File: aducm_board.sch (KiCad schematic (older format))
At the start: 49 parts, among them U1 aducm_355

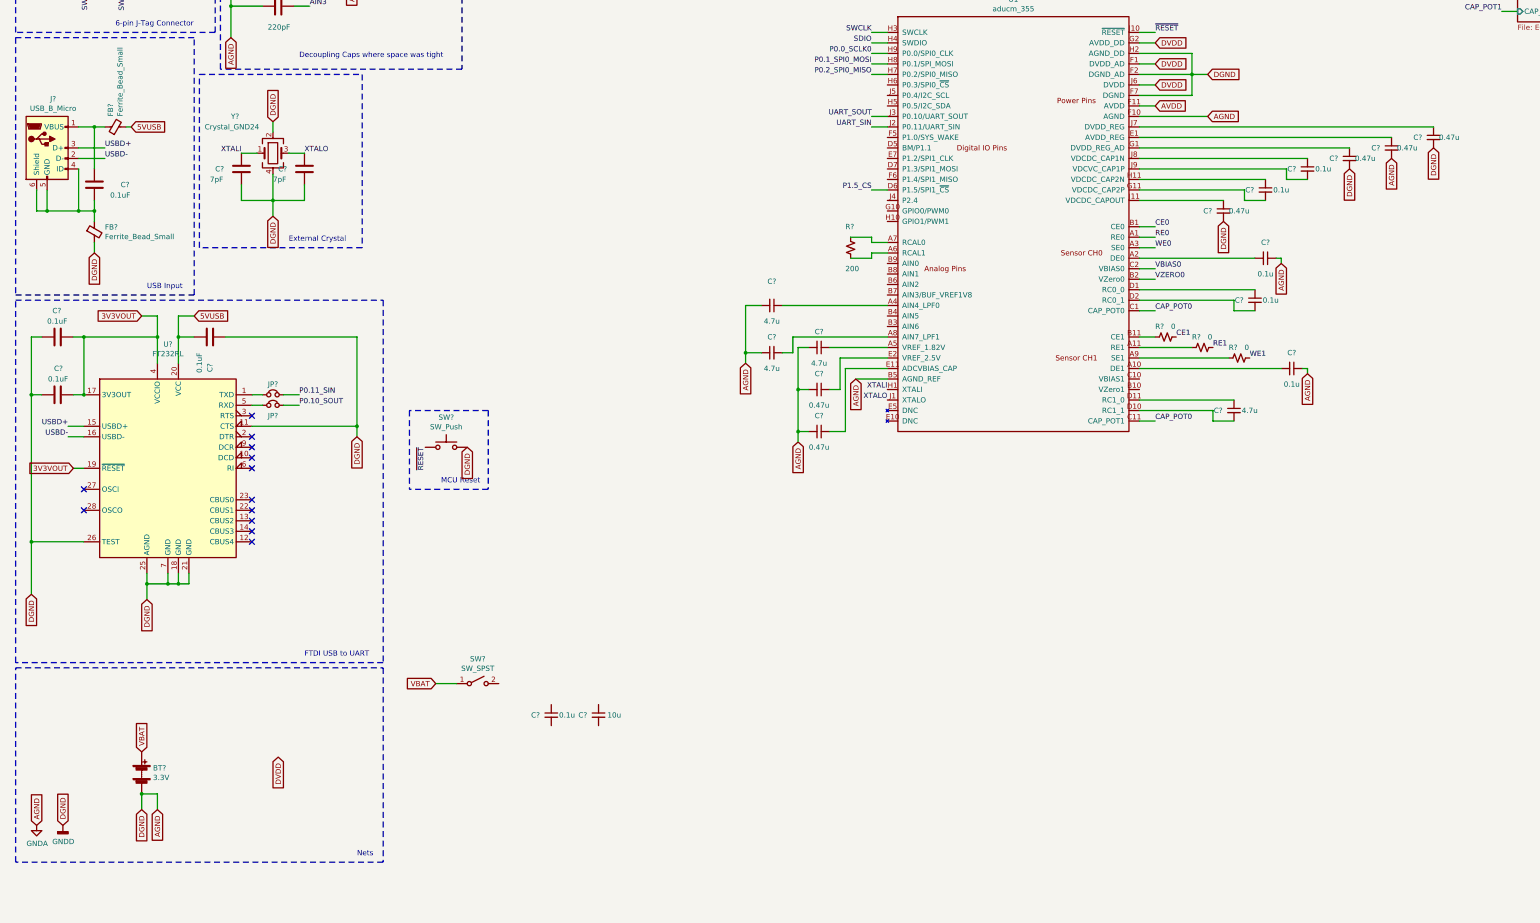
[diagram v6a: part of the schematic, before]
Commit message: Completed Power Supply Filtering
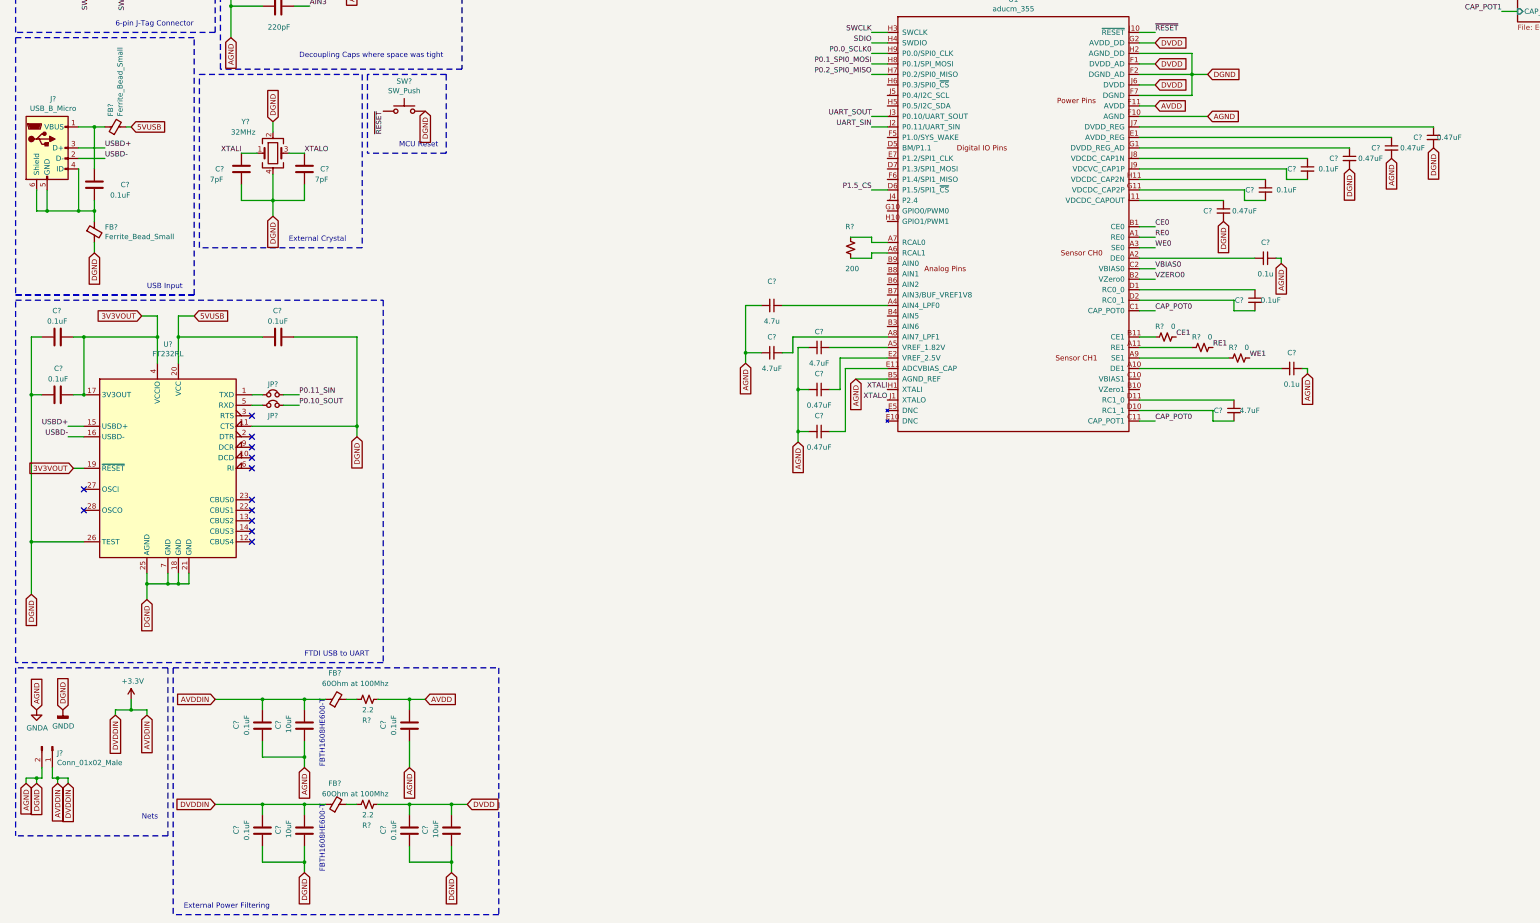
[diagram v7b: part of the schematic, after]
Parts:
- removed BT?: 3.3V, symbol Device:Battery
- removed C?: 0.1u, symbol Device:C_Small
- removed C?: 10u, symbol Device:C_Small
- removed SW?: SW_SPST, symbol Switch:SW_SPST
- added C? (x4): 0.1uF, symbol Device:C
- added C? (x3): 10uF, symbol Device:C
- added FB? (x2): 60Ohm at 100Mhz, symbol Device:Ferrite_Bead_Small
- added J?: Conn_01x02_Male, symbol Connector:Conn_01x02_Male
- added R? (x2): 2.2, symbol Device:R_Small_US
- C? (x6): value 0.47u -> 0.47uF
- C? (x3): value 4.7u -> 4.7uF
- C? (x3): value 0.1u -> 0.1uF
- Y?: value Crystal_GND24 -> 32MHz
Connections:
- net AVDD: now also C?.2, R?.1
- net DVDD: now also C?.2, C?.2, R?.1
- net GNDA: now also C?.1, C?.1, C?.1, C?.1, C?.1, C?.1, C?.1, J?.2 (Pin_2)
- new net: FB?.2, R?.2 (x2)
- new net +3V3: C?.2, C?.2, C?.2, C?.2, FB?.1, FB?.1, J?.1 (Pin_1)
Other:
- note added: "External Power Filtering"
- note added: "FBTH1608HE600-T"
- moved on the sheet: C?, SW?

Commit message: Working on power input
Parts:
- removed J?: Conn_01x02_Male, symbol Connector:Conn_01x02_Male
- added C43, C44: 0.1uF, Capacitor_SMD:C_0603_1608Metric, symbol Device:C
- added D1, D2: D_Schottky, symbol Device:D_Schottky
- added D3: LED, symbol Device:LED
- added J6: JST_PH, symbol Connector_Generic:Conn_01x02
- added R15: 2k, Resistor_SMD:R_0603_1608Metric, symbol Device:R_Small_US
- added R16: 440, Resistor_SMD:R_0603_1608Metric, symbol Device:R_Small_US
- added U3: SPX3819M5-L-3-3, Package_TO_SOT_SMD:SOT-23-5, symbol Regulator_Linear:SPX3819M5-L-3-3
- added U4: MCP73831-2-OT, Package_TO_SOT_SMD:SOT-23-5, symbol Battery_Management:MCP73831-2-OT
- C1, C10, C11, C12, C13, C14, C15, C16, C17, C18, C19, C2, C20, C21, C22, C23, C24, C25, C26, C27, C28, C29, C3, C30, C31, C32, C33, C34, C35, C36, C4, C5, C6, C7, C8, C9: renamed from C?; footprint (none) -> Capacitor_SMD:C_0603_1608Metric
- FB1, FB2, FB3, FB4: renamed from FB?; footprint (none) -> Inductor_SMD:L_0603_1608Metric
- J1: renamed from J?; footprint (none) -> Connector_USB:USB_Micro-B_Amphenol_10103594-0001LF_Horizontal
- J3: renamed from J?; footprint (none) -> Connector_PinHeader_2.54mm:PinHeader_2x04_P2.54mm_Horizontal
- R1, R2, R3, R4, R5, R6, R7, R8: renamed from R?; footprint (none) -> Resistor_SMD:R_0603_1608Metric
- SW1: renamed from SW?; footprint (none) -> Button_Switch_SMD:SW_SPST_B3S-1000
- U2: renamed from U?; footprint Package_SO:SSOP-28_5.3x10.2mm_P0.65mm -> Button_Switch_SMD:SW_SPST_B3S-1000
- gave numbers to parts that had none: 3
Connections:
- net 5VUSB: now also C43.1, R16.1, U4.4 (VDD)
- net GNDA: now also C43.2, C44.2, J6.1 (Pin_1), R15.1, U4.2 (VSS); no longer C1.2, C12.1, C13.2, C15.1, C16.2, C17.2, C2.1, C20.1, C21.1, C27.2, C34.2, C36.2, C4.2, C6.1, FB1.2, J3.2 (Pin_2), SW1.2, U1.F2 (DGND_AD), U1.F7 (DGND), U1.H2 (AGND_DD), U2.11 (CTS), U2.18 (GND), U2.21 (GND), U2.25 (AGND), U2.26 (TEST), U2.7 (GND), Y1.2, Y1.4
- net +3V3 renamed AVDDIN
- net AVDDIN: no longer C15.2, C6.2, FB4.1
- new net: D3.1 (K), U4.1 (STAT)
- new net: R15.2, U4.5 (PROG)
- new net: D3.2 (A), R16.2
- new net DVDDIN: C15.2, C6.2, FB4.1
- new net GNDD: C1.2, C12.1, C13.2, C15.1, C16.2, C17.2, C2.1, C20.1, C21.1, C27.2, C34.2, C36.2, C4.2, C6.1, FB1.2, J3.2 (Pin_2), SW1.2, U1.F2 (DGND_AD), U1.F7 (DGND), U1.H2 (AGND_DD), U2.11 (CTS), U2.18 (GND), U2.21 (GND), U2.25 (AGND), U2.26 (TEST), U2.7 (GND), Y1.2, Y1.4
- new net VBAT: C44.1, J6.2 (Pin_2), U4.3 (VBAT)
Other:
- note added: "Grounds"
- note added: "LiPo Battery Charging from USB"
- note added: "LiPo Battery Input"
- note removed: "Nets"
- moved on the sheet: C14, C15, C19, C20, C21, C5, C6, FB3, FB4, R3, R4
